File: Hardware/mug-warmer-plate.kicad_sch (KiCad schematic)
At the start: 29 parts, among them J1 USB_C_Receptacle, J4 Conn_01x02_Male, Q1 IRLZ44N, SW1 SW_DIP_x01, U1 LM35-NEB, U2 ATtiny85-20P

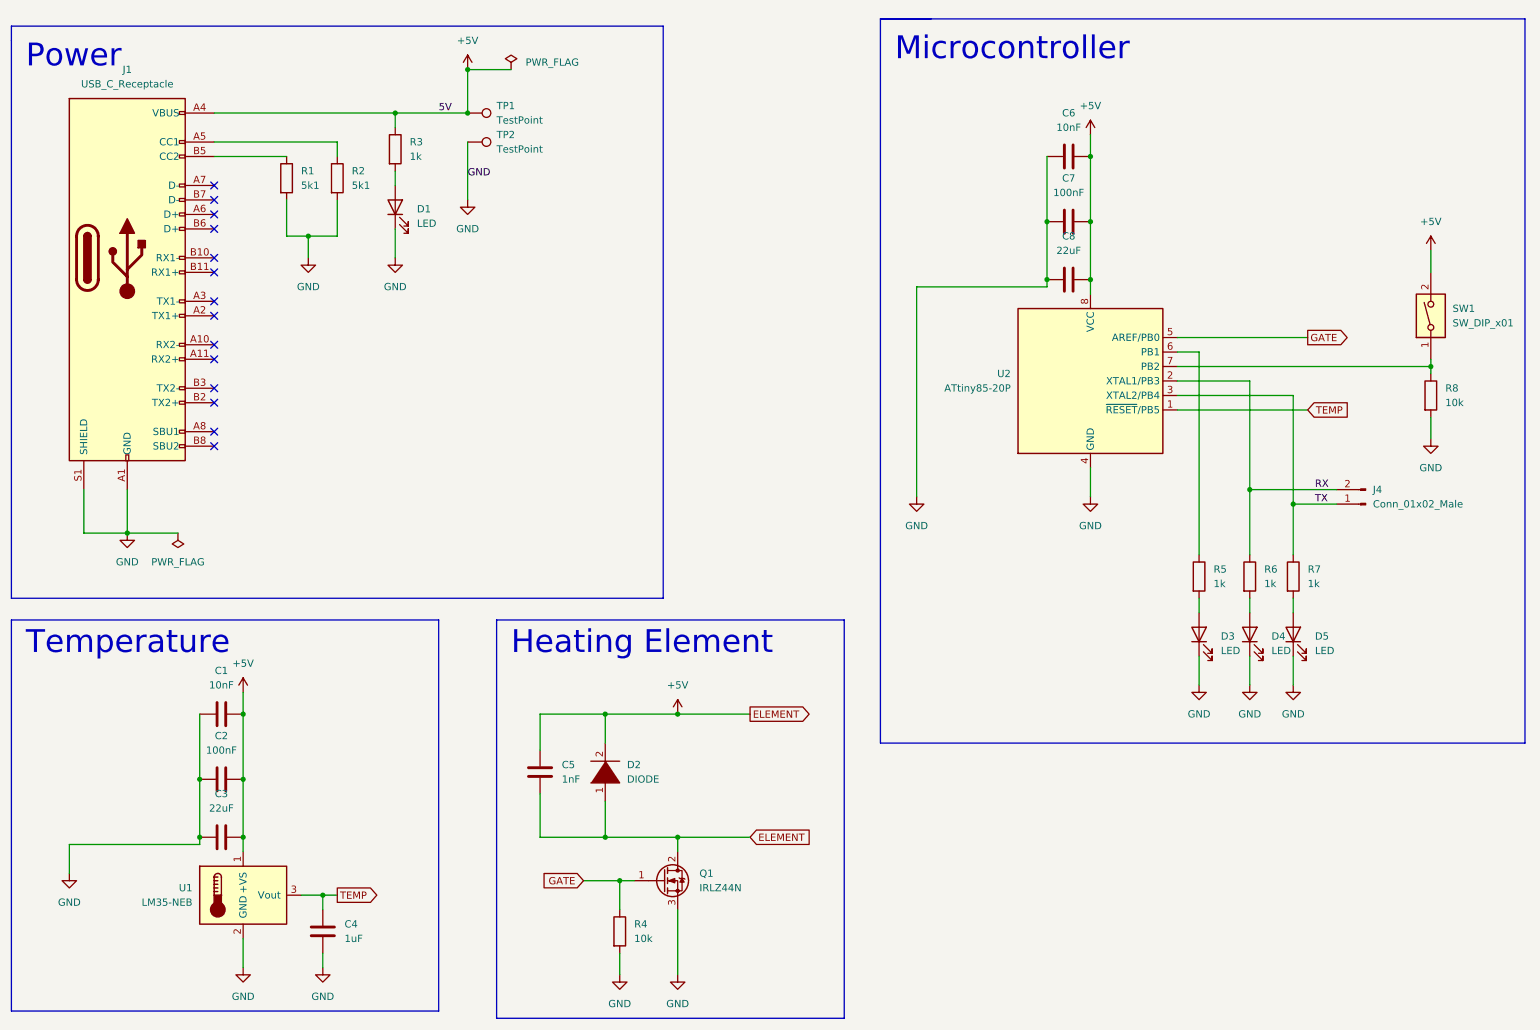
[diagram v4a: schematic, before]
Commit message: More fixes - Used 4 pin for serial communication i.e. 5v, RX, TX and GND - Remove GND and 5V net label to fix ERC warning
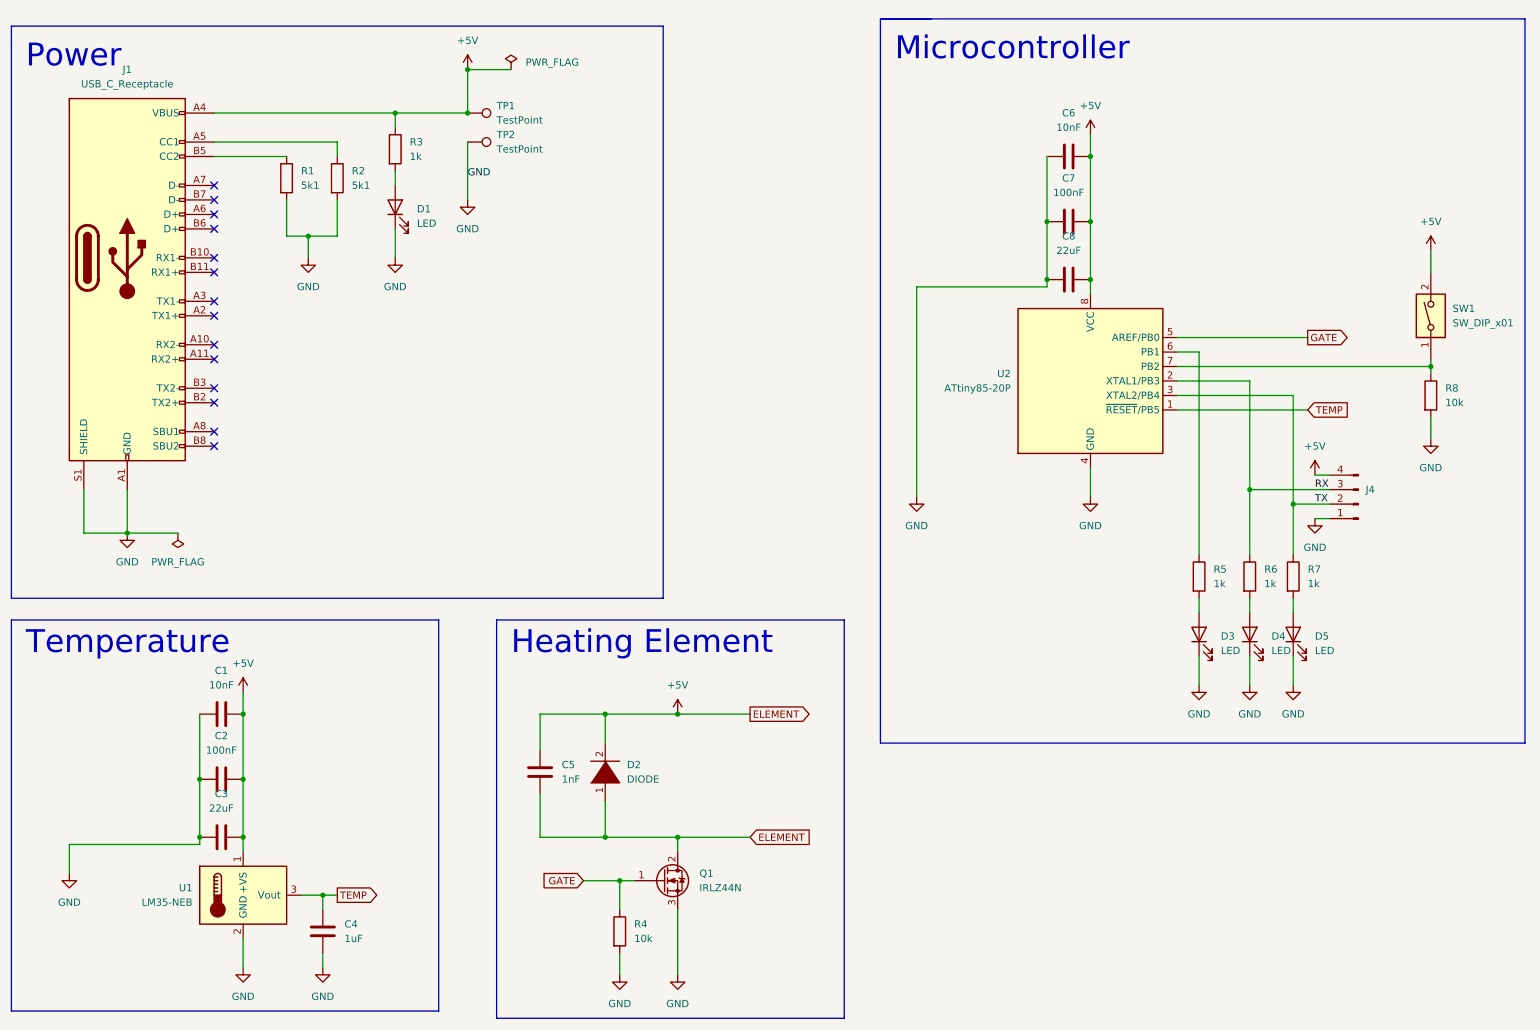
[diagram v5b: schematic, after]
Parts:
- J4: value Conn_01x02_Male -> (none); symbol Connector:Conn_01x02_Male -> Connector:Conn_01x04_Male
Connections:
- net +5V: now also J4.4 (Pin_4)
- net GND: now also J4.1 (Pin_1)
- net RX: now also J4.3 (Pin_3); no longer J4.2 (Pin_2)
- net TX: now also J4.2 (Pin_2); no longer J4.1 (Pin_1)
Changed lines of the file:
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@@
     (stroke (width 0) (type default) (color 0 0 0 0))
   )
-  (wire (pts (xy 242.57 104.14) (xy 250.19 104.14))
+  (wire (pts (xy 242.57 104.14) (xy 248.92 104.14))
     (stroke (width 0) (type default) (color 0 0 0 0))
   )
@@
     (stroke (width 0) (type default) (color 0 0 0 0))
   )
+  (wire (pts (xy 207.01 97.79) (xy 207.01 102.87))
+    (stroke (width 0) (type default) (color 0 0 0 0))
+  )
   (wire (pts (xy 226.06 77.47) (xy 226.06 113.03))
     (stroke (width 0) (type default) (color 0 0 0 0))
@@
     (stroke (width 0) (type default) (color 0 0 0 0))
   )
+  (wire (pts (xy 246.38 99.06) (xy 248.92 99.06))
+    (stroke (width 0) (type default) (color 0 0 0 0))
+  )
   (wire (pts (xy 266.7 80.01) (xy 266.7 78.74))
     (stroke (width 0) (type default) (color 0 0 0 0))
@@
     (stroke (width 0) (type default) (color 0 0 0 0))
   )
+  (wire (pts (xy 246.38 106.68) (xy 248.92 106.68))
+    (stroke (width 0) (type default) (color 0 0 0 0))
+  )
   (wire (pts (xy 234.95 130.81) (xy 234.95 135.89))
     (stroke (width 0) (type default) (color 0 0 0 0))
@@
     (stroke (width 0) (type default) (color 0 0 0 0))
   )
-  (wire (pts (xy 207.01 97.79) (xy 207.01 102.87))
-    (stroke (width 0) (type default) (color 0 0 0 0))
-  )
   (wire (pts (xy 27.94 163.83) (xy 50.8 163.83))
     (stroke (width 0) (type default) (color 0 0 0 0))
@@
     (stroke (width 0) (type default) (color 0 0 0 0))
   )
-  (wire (pts (xy 234.95 101.6) (xy 250.19 101.6))
+  (wire (pts (xy 234.95 101.6) (xy 248.92 101.6))
     (stroke (width 0) (type default) (color 0 0 0 0))
   )
@@
   )
   (label "GND" (at 97.79 46.99 0)
-    (effects (font (size 1.27 1.27)) (justify left bottom))
-  )
-  (label "5V" (at 92.71 35.56 0)
     (effects (font (size 1.27 1.27)) (justify left bottom))
   )
@@
     (pin "2")
   )
+  (symbol (lib_id "power:GND") (at 246.38 106.68 0) (unit 1)
+    (in_bom yes) (on_board yes) (fields_autoplaced)
+    (property "Reference" "#PWR0102" (id 0) (at 246.38 113.03 0)
+      (effects (font (size 1.27 1.27)) hide)
+    )
+    (property "Value" "GND" (id 1) (at 246.38 111.76 0))
+    (property "Footprint" "" (id 2) (at 246.38 106.68 0)
+      (effects (font (size 1.27 1.27)) hide)
+    )
+    (property "Datasheet" "" (id 3) (at 246.38 106.68 0)
+      (effects (font (size 1.27 1.27)) hide)
+    )
+    (pin "1")
+  )
   (symbol (lib_id "Device:C") (at 54.61 140.97 90) (unit 1)
     (in_bom yes) (on_board yes) (fields_autoplaced)
@@
     (pin "1")
   )
-  (symbol (lib_id "Connector:Conn_01x02_Male") (at 255.27 104.14 180) (unit 1)
-    (in_bom yes) (on_board yes) (fields_autoplaced)
-    (property "Reference" "J4" (id 0) (at 256.54 101.5999 0)
-      (effects (font (size 1.27 1.27)) (justify right))
-    )
-    (property "Value" "Conn_01x02_Male" (id 1) (at 256.54 104.1399 0)
-      (effects (font (size 1.27 1.27)) (justify right))
-    )
-    (property "Footprint" "" (id 2) (at 255.27 104.14 0)
-      (effects (font (size 1.27 1.27)) hide)
-    )
-    (property "Datasheet" "~" (id 3) (at 255.27 104.14 0)
-      (effects (font (size 1.27 1.27)) hide)
-    )
-    (pin "1")
-    (pin "2")
+  (symbol (lib_id "Connector:Conn_01x04_Male") (at 254 104.14 180) (unit 1)
+    (in_bom yes) (on_board yes) (fields_autoplaced)
+    (property "Reference" "J4" (id 0) (at 255.27 101.5999 0)
+      (effects (font (size 1.27 1.27)) (justify right))
+    )
+    (property "Value" "" (id 1) (at 255.27 104.1399 0)
+      (effects (font (size 1.27 1.27)) (justify right))
+    )
+    (property "Footprint" "" (id 2) (at 254 104.14 0)
+      (effects (font (size 1.27 1.27)) hide)
+    )
+    (property "Datasheet" "~" (id 3) (at 254 104.14 0)
+      (effects (font (size 1.27 1.27)) hide)
+    )
+    (pin "1")
+    (pin "2")
+    (pin "3")
+    (pin "4")
   )
   (symbol (lib_id "power:GND") (at 266.7 92.71 0) (unit 1)
@@
     (pin "2")
   )
+  (symbol (lib_id "power:+5V") (at 246.38 99.06 0) (unit 1)
+    (in_bom yes) (on_board yes)
+    (property "Reference" "#PWR0101" (id 0) (at 246.38 102.87 0)
+      (effects (font (size 1.27 1.27)) hide)
+    )
+    (property "Value" "+5V" (id 1) (at 246.38 93.98 0))
+    (property "Footprint" "" (id 2) (at 246.38 99.06 0)
+      (effects (font (size 1.27 1.27)) hide)
+    )
+    (property "Datasheet" "" (id 3) (at 246.38 99.06 0)
+      (effects (font (size 1.27 1.27)) hide)
+    )
+    (pin "1")
+  )
   (sheet_instances
     (path "/" (page "1"))
@@
       (reference "#PWR020") (unit 1) (value "GND") (footprint "")
     )
+    (path "/fa1d3d41-de91-4607-87ae-3b485de979cc"
+      (reference "#PWR0101") (unit 1) (value "+5V") (footprint "")
+    )
+    (path "/426559ac-df1a-47bd-8757-fd461a7fb2ff"
+      (reference "#PWR0102") (unit 1) (value "GND") (footprint "")
+    )
     (path "/43dad61f-0b42-4b9c-924b-b6f12961779e"
       (reference "C1") (unit 1) (value "10nF") (footprint "Capacitor_THT:C_Disc_D4.3mm_W1.9mm_P5.00mm")
@@
     )
     (path "/5421082f-59cf-46ec-9af9-318fc95f62cc"
-      (reference "J4") (unit 1) (value "Conn_01x02_Male") (footprint "Connector_PinHeader_2.54mm:PinHeader_1x02_P2.54mm_Vertical")
+      (reference "J4") (unit 1) (value "Conn_01x02_Male") (footprint "Connector_PinHeader_2.54mm:PinHeader_1x04_P2.54mm_Vertical")
     )
     (path "/c229fabb-c04a-4bb3-af27-16bead0c0502"

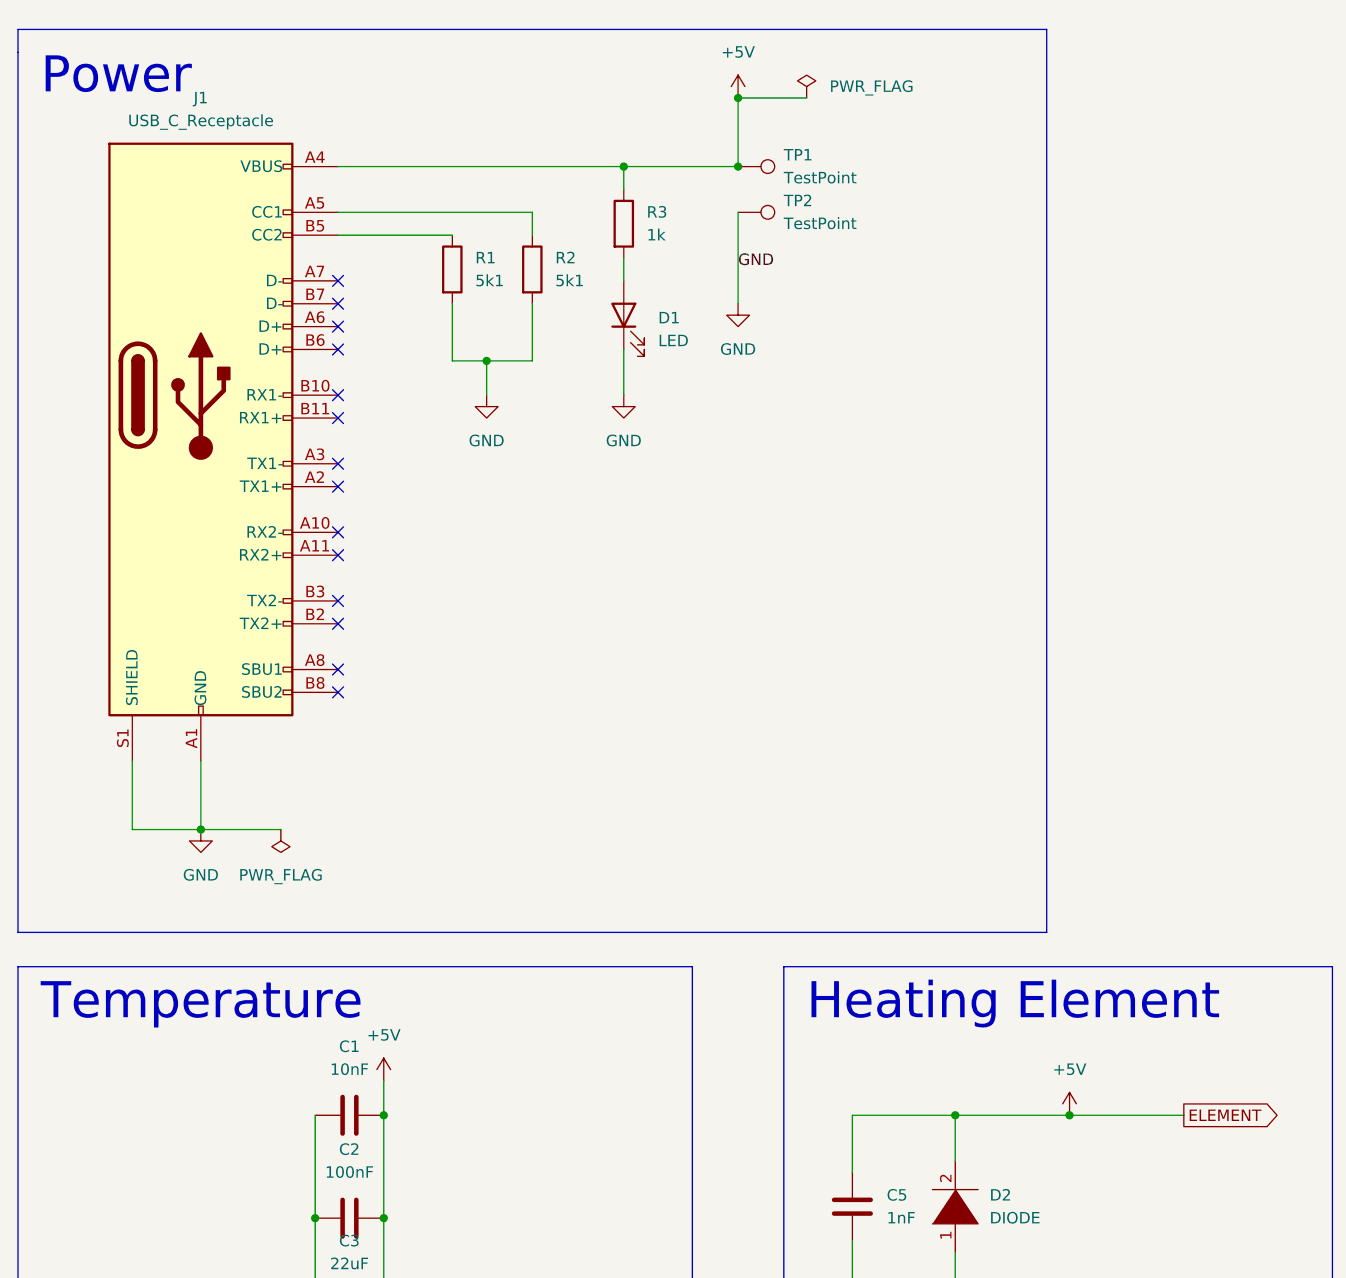
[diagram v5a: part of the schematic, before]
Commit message: Fix USB_C_Receptacle and ELEMENT net - Replace with USB_C_Receptacle_USB2.0 for smaller footprint in sheet - Added NetTie symbol and footprint to clearly differentiate ELEMENT net
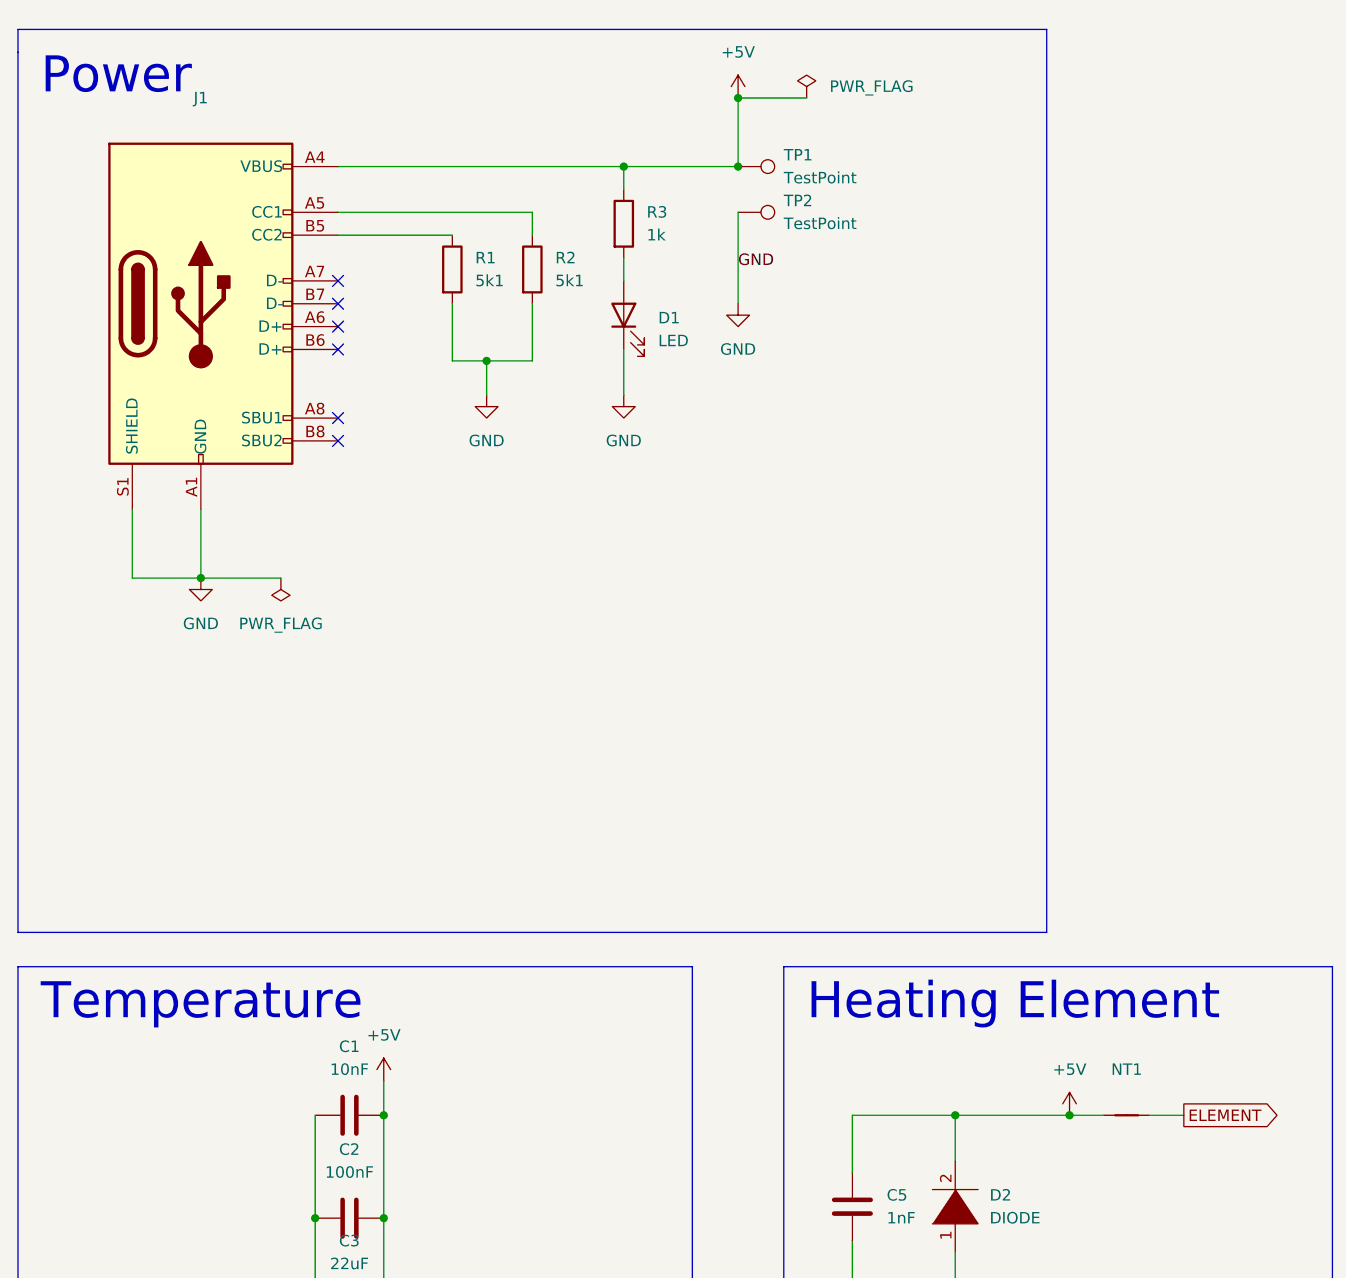
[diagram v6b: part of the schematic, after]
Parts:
- removed J1: USB_C_Receptacle, symbol Connector:USB_C_Receptacle
- added J1: (no value), symbol Connector:USB_C_Receptacle_USB2.0
- added NT1: (no value), symbol Device:NetTie_2
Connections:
- net +5V: now also J1.A4 (VBUS), J1.A9 (VBUS), J1.B4 (VBUS), J1.B9 (VBUS), NT1.1; no longer C5.1, D2.1 (K), Q1.2 (D)
- net GND: now also J1.A1 (GND), J1.A12 (GND), J1.B1 (GND), J1.B12 (GND), J1.S1 (SHIELD)
- net at R1.1: now also J1.B5 (CC2)
- net at R2.1: now also J1.A5 (CC1)
- new net ELEMENT: C5.1, D2.1 (K), NT1.2, Q1.2 (D)
- no-connect marks 14 -> 6
